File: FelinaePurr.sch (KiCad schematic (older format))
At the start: 21 parts, among them P1 USB_OTG, P2 JACK, U1 FT232RL, U2 SN74LVC1G126-Q1

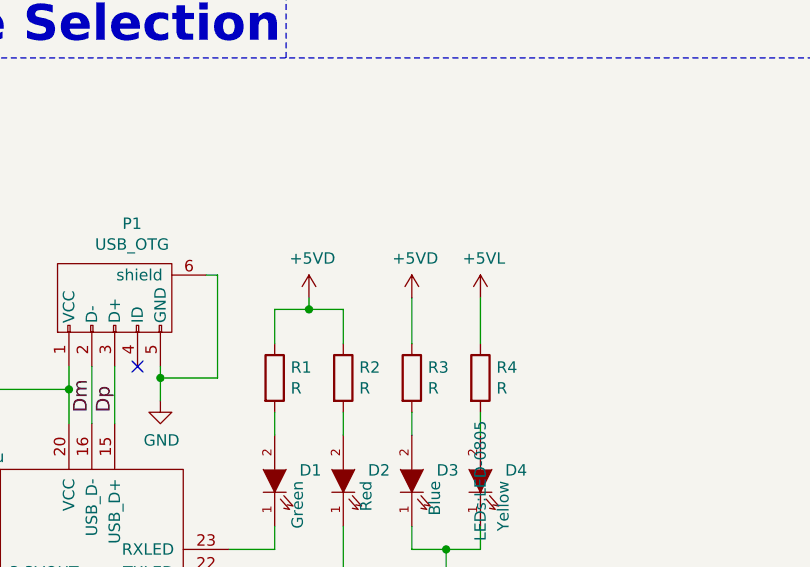
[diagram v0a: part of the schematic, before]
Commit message: Update R on D2/D4 to use two 100Ω R and add value for D1/D2 R
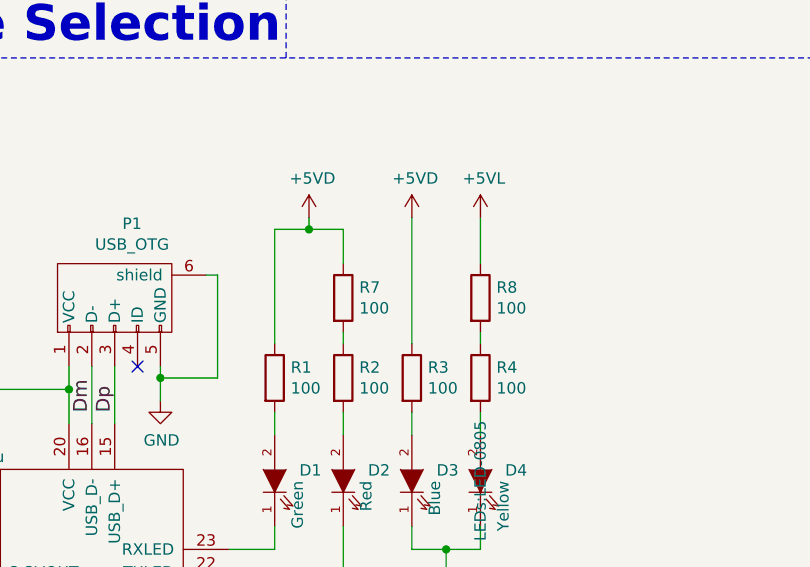
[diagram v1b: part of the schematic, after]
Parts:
- added R7, R8: 100, Resistors_SMD:R_0603, symbol R
- R1, R2, R3, R4: value R -> 100
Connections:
- net +5VD: now also R7.1; no longer R2.1
- net +5VL: now also R8.1; no longer R4.1
- new net: R2.1, R7.2
- new net: R4.1, R8.2
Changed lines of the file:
@@
 $EndComp
 $Comp
-L +5V #PWR01
+L +5V #PWR4
 U 1 1 5788C03E
 P 2500 1550
-F 0 "#PWR01" H 2500 1400 50  0001 C CNN
+F 0 "#PWR4" H 2500 1400 50  0001 C CNN
 F 1 "+5V" H 2515 1723 50  0000 C CNN
 F 2 "" H 2500 1550 50  0000 C CNN
@@
 $EndComp
 $Comp
-L +5VD #PWR02
+L +5VD #PWR2
 U 1 1 5788C095
 P 2150 1750
-F 0 "#PWR02" H 2150 1600 50  0001 C CNN
+F 0 "#PWR2" H 2150 1600 50  0001 C CNN
 F 1 "+5VD" H 2165 1923 50  0000 C CNN
 F 2 "" H 2150 1750 50  0000 C CNN
@@
 $EndComp
 $Comp
-L +5VL #PWR03
+L +5VL #PWR7
 U 1 1 5788C0B2
 P 2850 1750
-F 0 "#PWR03" H 2850 1600 50  0001 C CNN
+F 0 "#PWR7" H 2850 1600 50  0001 C CNN
 F 1 "+5VL" H 2865 1923 50  0000 C CNN
 F 2 "" H 2850 1750 50  0000 C CNN
@@
 $EndComp
 $Comp
-L PWR_FLAG #FLG04
+L PWR_FLAG #FLG1
 U 1 1 5788C17B
 P 2450 1750
-F 0 "#FLG04" H 2450 1845 50  0001 C CNN
+F 0 "#FLG1" H 2450 1845 50  0001 C CNN
 F 1 "PWR_FLAG" V 2750 1800 50  0000 L CNN
 F 2 "" H 2450 1750 50  0000 C CNN
@@
 $EndComp
 $Comp
-L +5VL #PWR05
+L +5VL #PWR19
 U 1 1 5788C270
 P 9050 4650
-F 0 "#PWR05" H 9050 4500 50  0001 C CNN
+F 0 "#PWR19" H 9050 4500 50  0001 C CNN
 F 1 "+5VL" H 9065 4823 50  0000 C CNN
 F 2 "" H 9050 4650 50  0000 C CNN
@@
 $EndComp
 $Comp
-L GND #PWR06
+L GND #PWR20
 U 1 1 5788C2A8
 P 9050 5050
-F 0 "#PWR06" H 9050 4800 50  0001 C CNN
+F 0 "#PWR20" H 9050 4800 50  0001 C CNN
 F 1 "GND" H 9055 4877 50  0000 C CNN
 F 2 "" H 9050 5050 50  0000 C CNN
@@
 TIP\nINNER\nBASE
 $Comp
-L PWR_FLAG #FLG07
+L PWR_FLAG #FLG2
 U 1 1 5788C38F
 P 8850 4750
-F 0 "#FLG07" H 8850 4845 50  0001 C CNN
+F 0 "#FLG2" H 8850 4845 50  0001 C CNN
 F 1 "PWR_FLAG" V 8850 4928 50  0000 L CNN
 F 2 "" H 8850 4750 50  0000 C CNN
@@
 $EndComp
 $Comp
-L GND #PWR08
+L GND #PWR16
 U 1 1 5788C66D
 P 7250 2300
-F 0 "#PWR08" H 7250 2050 50  0001 C CNN
+F 0 "#PWR16" H 7250 2050 50  0001 C CNN
 F 1 "GND" H 7255 2127 50  0000 C CNN
 F 2 "" H 7250 2300 50  0000 C CNN
@@
 $EndComp
 $Comp
-L +5VD #PWR09
+L +5VD #PWR5
 U 1 1 5788CC48
 P 2500 4250
-F 0 "#PWR09" H 2500 4100 50  0001 C CNN
+F 0 "#PWR5" H 2500 4100 50  0001 C CNN
 F 1 "+5VD" H 2515 4423 50  0000 C CNN
 F 2 "" H 2500 4250 50  0000 C CNN
@@
 $EndComp
 $Comp
-L GND #PWR010
+L GND #PWR9
 U 1 1 5788CC92
 P 3800 4450
-F 0 "#PWR010" H 3800 4200 50  0001 C CNN
+F 0 "#PWR9" H 3800 4200 50  0001 C CNN
 F 1 "GND" H 3805 4277 50  0000 C CNN
 F 2 "" H 3800 4450 50  0000 C CNN
@@
 $EndComp
 $Comp
-L GND #PWR011
+L GND #PWR3
 U 1 1 5788D07A
 P 2450 6100
-F 0 "#PWR011" H 2450 5850 50  0001 C CNN
+F 0 "#PWR3" H 2450 5850 50  0001 C CNN
 F 1 "GND" H 2455 5927 50  0000 C CNN
 F 2 "" H 2450 6100 50  0000 C CNN
@@
 $EndComp
 $Comp
-L GND #PWR012
+L GND #PWR1
 U 1 1 5788D0D6
 P 1600 5800
-F 0 "#PWR012" H 1600 5550 50  0001 C CNN
+F 0 "#PWR1" H 1600 5550 50  0001 C CNN
 F 1 "GND" H 1605 5627 50  0000 C CNN
 F 2 "" H 1600 5800 50  0000 C CNN
@@
 P 4300 4350
 F 0 "R1" H 4370 4396 50  0000 L CNN
-F 1 "R" H 4370 4305 50  0000 L CNN
+F 1 "100" H 4370 4305 50  0000 L CNN
 F 2 "Resistors_SMD:R_0603" V 4230 4350 50  0001 C CNN
 F 3 "" H 4300 4350 50  0000 C CNN
@@
 P 4600 4350
 F 0 "R2" H 4670 4396 50  0000 L CNN
-F 1 "R" H 4670 4305 50  0000 L CNN
+F 1 "100" H 4670 4305 50  0000 L CNN
 F 2 "Resistors_SMD:R_0603" V 4530 4350 50  0001 C CNN
 F 3 "" H 4600 4350 50  0000 C CNN
@@
 $EndComp
 $Comp
-L +5VD #PWR013
+L +5VD #PWR10
 U 1 1 5788D588
-P 4450 4000
-F 0 "#PWR013" H 4450 3850 50  0001 C CNN
-F 1 "+5VD" H 4465 4173 50  0000 C CNN
-F 2 "" H 4450 4000 50  0000 C CNN
-F 3 "" H 4450 4000 50  0000 C CNN
-	1    4450 4000
+P 4450 3650
+F 0 "#PWR10" H 4450 3500 50  0001 C CNN
+F 1 "+5VD" H 4465 3823 50  0000 C CNN
+F 2 "" H 4450 3650 50  0000 C CNN
+F 3 "" H 4450 3650 50  0000 C CNN
+	1    4450 3650
 	1    0    0    -1
 $EndComp
@@
 P 4900 4350
 F 0 "R3" H 4970 4396 50  0000 L CNN
-F 1 "R" H 4970 4305 50  0000 L CNN
+F 1 "100" H 4970 4305 50  0000 L CNN
 F 2 "Resistors_SMD:R_0603" V 4830 4350 50  0001 C CNN
 F 3 "" H 4900 4350 50  0000 C CNN
@@
 P 5200 4350
 F 0 "R4" H 5270 4396 50  0000 L CNN
-F 1 "R" H 5270 4305 50  0000 L CNN
+F 1 "100" H 5270 4305 50  0000 L CNN
 F 2 "Resistors_SMD:R_0603" V 5130 4350 50  0001 C CNN
 F 3 "" H 5200 4350 50  0000 C CNN
@@
 $EndComp
 $Comp
-L GND #PWR014
+L GND #PWR12
 U 1 1 5788DEA1
 P 5050 5200
-F 0 "#PWR014" H 5050 4950 50  0001 C CNN
+F 0 "#PWR12" H 5050 4950 50  0001 C CNN
 F 1 "GND" H 5055 5027 50  0000 C CNN
 F 2 "" H 5050 5200 50  0000 C CNN
@@
 $EndComp
 $Comp
-L +5VD #PWR015
+L +5VD #PWR11
 U 1 1 5788E141
-P 4900 4000
-F 0 "#PWR015" H 4900 3850 50  0001 C CNN
-F 1 "+5VD" H 4915 4173 50  0000 C CNN
-F 2 "" H 4900 4000 50  0000 C CNN
-F 3 "" H 4900 4000 50  0000 C CNN
-	1    4900 4000
-	1    0    0    -1
-$EndComp
-$Comp
-L +5VL #PWR016
+P 4900 3650
+F 0 "#PWR11" H 4900 3500 50  0001 C CNN
+F 1 "+5VD" H 4915 3823 50  0000 C CNN
+F 2 "" H 4900 3650 50  0000 C CNN
+F 3 "" H 4900 3650 50  0000 C CNN
+	1    4900 3650
+	1    0    0    -1
+$EndComp
+$Comp
+L +5VL #PWR13
 U 1 1 5788E182
-P 5200 4000
-F 0 "#PWR016" H 5200 3850 50  0001 C CNN
-F 1 "+5VL" H 5215 4173 50  0000 C CNN
-F 2 "" H 5200 4000 50  0000 C CNN
-F 3 "" H 5200 4000 50  0000 C CNN
-	1    5200 4000
+P 5200 3650
+F 0 "#PWR13" H 5200 3500 50  0001 C CNN
+F 1 "+5VL" H 5215 3823 50  0000 C CNN
+F 2 "" H 5200 3650 50  0000 C CNN
+F 3 "" H 5200 3650 50  0000 C CNN
+	1    5200 3650
 	1    0    0    -1
 $EndComp
@@
 $EndComp
 $Comp
-L GND #PWR017
+L GND #PWR8
 U 1 1 5788ECC9
 P 2850 4900
-F 0 "#PWR017" H 2850 4650 50  0001 C CNN
+F 0 "#PWR8" H 2850 4650 50  0001 C CNN
 F 1 "GND" H 2855 4727 50  0000 C CNN
 F 2 "" H 2850 4900 50  0000 C CNN
@@
 $EndComp
 $Comp
-L GND #PWR018
+L GND #PWR14
 U 1 1 5788F1B2
 P 5550 2150
-F 0 "#PWR018" H 5550 1900 50  0001 C CNN
+F 0 "#PWR14" H 5550 1900 50  0001 C CNN
 F 1 "GND" H 5555 1977 50  0000 C CNN
 F 2 "" H 5550 2150 50  0000 C CNN
@@
 $EndComp
 $Comp
-L GND #PWR019
+L GND #PWR18
 U 1 1 5788FD51
 P 8950 2450
-F 0 "#PWR019" H 8950 2200 50  0001 C CNN
+F 0 "#PWR18" H 8950 2200 50  0001 C CNN
 F 1 "GND" H 8955 2277 50  0000 C CNN
 F 2 "" H 8950 2450 50  0000 C CNN
@@
 $EndComp
 $Comp
-L +5V #PWR020
+L +5V #PWR17
 U 1 1 5788FE88
 P 8950 1300
-F 0 "#PWR020" H 8950 1150 50  0001 C CNN
+F 0 "#PWR17" H 8950 1150 50  0001 C CNN
 F 1 "+5V" H 8965 1473 50  0000 C CNN
 F 2 "" H 8950 1300 50  0000 C CNN
@@
 $EndComp
 $Comp
-L +5V #PWR021
+L +5V #PWR15
 U 1 1 5788FEE9
 P 6050 1600
-F 0 "#PWR021" H 6050 1450 50  0001 C CNN
+F 0 "#PWR15" H 6050 1450 50  0001 C CNN
 F 1 "+5V" H 6065 1773 50  0000 C CNN
 F 2 "" H 6050 1600 50  0000 C CNN
@@
 $EndComp
 $Comp
-L +5V #PWR022
+L +5V #PWR6
 U 1 1 5789013C
 P 2550 5100
-F 0 "#PWR022" H 2550 4950 50  0001 C CNN
+F 0 "#PWR6" H 2550 4950 50  0001 C CNN
 F 1 "+5V" H 2565 5273 50  0000 C CNN
 F 2 "" H 2550 5100 50  0000 C CNN
@@
 	4100 5350 4750 5350
 Wire Wire Line
-	5200 4200 5200 4000
-Wire Wire Line
-	4900 4000 4900 4200
+	5200 3850 5200 3650
+Wire Wire Line
+	4900 3650 4900 4200
 Wire Wire Line
 	5200 4500 5200 4600
@@
 Wire Wire Line
 	4300 4500 4300 4600
-Connection ~ 4450 4050
-Wire Wire Line
-	4450 4000 4450 4050
-Wire Wire Line
-	4300 4050 4600 4050
-Wire Wire Line
-	4600 4050 4600 4200
-Wire Wire Line
-	4300 4200 4300 4050
+Connection ~ 4450 3700
+Wire Wire Line
+	4450 3650 4450 3700
+Wire Wire Line
+	4300 3700 4600 3700
+Wire Wire Line
+	4600 3700 4600 3850
+Wire Wire Line
+	4300 3700 4300 4200
 Wire Wire Line
 	1600 5600 1600 5800
@@
 	2500 1550 2500 1850
 $Comp
-L PWR_FLAG #FLG023
+L PWR_FLAG #FLG3
 U 1 1 57891E0F
 P 8850 4950
-F 0 "#FLG023" H 8850 5045 50  0001 C CNN
+F 0 "#FLG3" H 8850 5045 50  0001 C CNN
 F 1 "PWR_FLAG" V 8850 5128 50  0000 L CNN
 F 2 "" H 8850 4950 50  0000 C CNN
@@
 	2100 5700 1600 5700
 Connection ~ 1600 5700
+$Comp
+L R R7
+U 1 1 578954EA
+P 4600 4000
+F 0 "R7" H 4670 4046 50  0000 L CNN
+F 1 "100" H 4670 3955 50  0000 L CNN
+F 2 "Resistors_SMD:R_0603" V 4530 4000 50  0001 C CNN
+F 3 "" H 4600 4000 50  0000 C CNN
+	1    4600 4000
+	1    0    0    -1
+$EndComp
+Wire Wire Line
+	4600 4150 4600 4200
+$Comp
+L R R8
+U 1 1 578956B8
+P 5200 4000
+F 0 "R8" H 5270 4046 50  0000 L CNN
+F 1 "100" H 5270 3955 50  0000 L CNN
+F 2 "Resistors_SMD:R_0603" V 5130 4000 50  0001 C CNN
+F 3 "" H 5200 4000 50  0000 C CNN
+	1    5200 4000
+	1    0    0    -1
+$EndComp
+Wire Wire Line
+	5200 4150 5200 4200
 $EndSCHEMATC

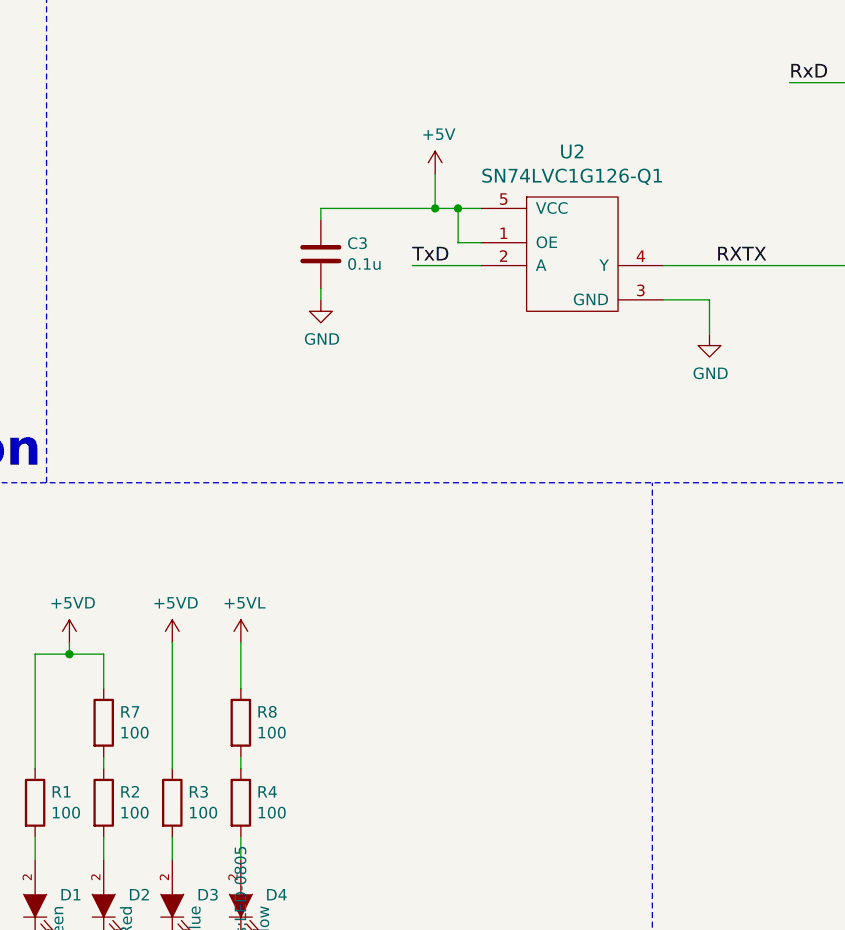
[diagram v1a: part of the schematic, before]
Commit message: Correct a stupid error on U2 and add 100Ω more to the blue led which is clearly too bright
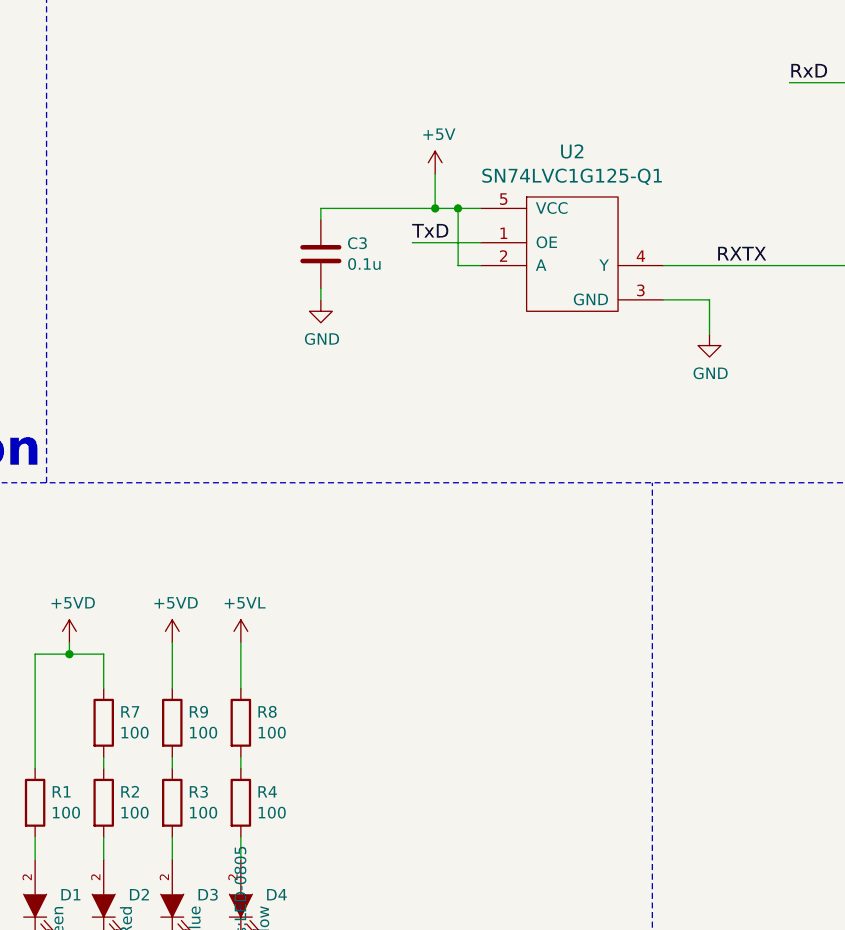
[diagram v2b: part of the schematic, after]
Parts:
- removed U2: SN74LVC1G126-Q1, TO_SOT_Packages_SMD:SOT-23-5, symbol SN74LVC1G126-Q1
- added R9: 100, Resistors_SMD:R_0603, symbol R
- added U2: SN74LVC1G125-Q1, TO_SOT_Packages_SMD:SOT-23-5, symbol SN74LVC1G125-Q1
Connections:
- net +5V: now also U2.2 (A), U2.5 (VCC)
- net +5VD: now also R9.1; no longer R3.1
- net GND: now also U2.3 (GND)
- net RXTX: now also U2.4 (Y)
- net TxD: now also U2.1 (OE)
- new net: R3.1, R9.2
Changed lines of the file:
@@
 LIBS:sn74lvc1g126-q1
 LIBS:ft232rl
+LIBS:sn74lvc1g125-q1
 LIBS:FelinaePurr-cache
 EELAYER 25 0
@@
 $EndComp
 $Comp
-L SN74LVC1G126-Q1 U2
-U 1 1 5788C59F
-P 6650 2000
-F 0 "U2" H 6650 2497 60  0000 C CNN
-F 1 "SN74LVC1G126-Q1" H 6650 2391 60  0000 C CNN
-F 2 "TO_SOT_Packages_SMD:SOT-23-5" H 6650 1900 60  0001 C CNN
-F 3 "" H 6650 1900 60  0001 C CNN
-	1    6650 2000
-	1    0    0    -1
-$EndComp
-$Comp
 L GND #PWR16
 U 1 1 5788C66D
@@
 	1    0    0    -1
 $EndComp
-Text Label 5950 2000 0    60   ~ 0
+Text Label 5950 1900 0    60   ~ 0
 TxD
 $Comp
@@
 Wire Wire Line
 	8750 2000 9550 2000
-Wire Wire Line
-	6250 2000 5950 2000
 Connection ~ 6150 1750
 Wire Wire Line
-	6150 1750 6150 1900
-Wire Wire Line
-	6150 1900 6250 1900
+	6150 1750 6150 2000
 Wire Wire Line
 	5550 2100 5550 2150
@@
 Wire Wire Line
 	5200 3850 5200 3650
-Wire Wire Line
-	4900 3650 4900 4200
 Wire Wire Line
 	5200 4500 5200 4600
@@
 Wire Wire Line
 	5200 4150 5200 4200
+$Comp
+L SN74LVC1G125-Q1 U2
+U 1 1 58FCCB54
+P 6650 2000
+F 0 "U2" H 6650 2497 60  0000 C CNN
+F 1 "SN74LVC1G125-Q1" H 6650 2391 60  0000 C CNN
+F 2 "TO_SOT_Packages_SMD:SOT-23-5" H 6650 1900 60  0001 C CNN
+F 3 "" H 6650 1900 60  0001 C CNN
+	1    6650 2000
+	1    0    0    -1
+$EndComp
+Wire Wire Line
+	6150 2000 6250 2000
+Wire Wire Line
+	5950 1900 6250 1900
+$Comp
+L R R9
+U 1 1 58FCD045
+P 4900 4000
+F 0 "R9" H 4970 4046 50  0000 L CNN
+F 1 "100" H 4970 3955 50  0000 L CNN
+F 2 "Resistors_SMD:R_0603" V 4830 4000 50  0001 C CNN
+F 3 "" H 4900 4000 50  0000 C CNN
+	1    4900 4000
+	1    0    0    -1
+$EndComp
+Wire Wire Line
+	4900 3850 4900 3650
+Wire Wire Line
+	4900 4150 4900 4200
 $EndSCHEMATC

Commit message: Another stupid mistake corrected..
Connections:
- net +5V: no longer U2.2 (A)
- net GND: now also U2.2 (A)
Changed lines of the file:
@@
 Wire Wire Line
 	8750 2000 9550 2000
-Connection ~ 6150 1750
-Wire Wire Line
-	6150 1750 6150 2000
 Wire Wire Line
 	5550 2100 5550 2150
@@
 Wire Wire Line
 	4900 4150 4900 4200
+$Comp
+L GND #PWR?
+U 1 1 58FD2FCD
+P 6150 2150
+F 0 "#PWR?" H 6150 1900 50  0001 C CNN
+F 1 "GND" H 6155 1977 50  0000 C CNN
+F 2 "" H 6150 2150 50  0000 C CNN
+F 3 "" H 6150 2150 50  0000 C CNN
+	1    6150 2150
+	1    0    0    -1
+$EndComp
+Wire Wire Line
+	6150 2150 6150 2000
 $EndSCHEMATC
